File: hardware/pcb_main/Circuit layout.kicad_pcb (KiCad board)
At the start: 4 copper layers, 0 parts

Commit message: Bridges done, main layout done
layer pours done
CHanged zif connector to 8 wide to the bridge
Changed voltage levels
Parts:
- added C1: 1uF, Capacitor_SMD:C_0402_1005Metric_Pad0.74x0.62mm_HandSolder, F.Cu at (108.6, 105.3)
- added C10: 4.7nF, Capacitor_SMD:C_0402_1005Metric_Pad0.74x0.62mm_HandSolder, F.Cu at (82.2, 119.8)
- added C11: 4.7nF, Capacitor_SMD:C_0402_1005Metric_Pad0.74x0.62mm_HandSolder, F.Cu at (80.2, 119.8)
- added C12: 100nF, Capacitor_SMD:C_0402_1005Metric_Pad0.74x0.62mm_HandSolder, F.Cu at (93.0, 122.5)
- added C13: 10uF, Capacitor_SMD:C_0402_1005Metric_Pad0.74x0.62mm_HandSolder, F.Cu at (94.0, 122.5)
- added C14: 1uF, Capacitor_SMD:C_0402_1005Metric_Pad0.74x0.62mm_HandSolder, F.Cu at (95.0, 122.5)
- added C15: 100uF, Capacitor_SMD:C_0805_2012Metric_Pad1.18x1.45mm_HandSolder, F.Cu at (97.5, 122.3)
- added C16: 1uF, Capacitor_SMD:C_0402_1005Metric_Pad0.74x0.62mm_HandSolder, F.Cu at (100.0, 122.4)
- added C17: 1.5nF, Capacitor_SMD:C_0402_1005Metric_Pad0.74x0.62mm_HandSolder, F.Cu at (91.0, 107.0)
- added C18: 100nF, Capacitor_SMD:C_0402_1005Metric_Pad0.74x0.62mm_HandSolder, F.Cu at (96.5, 107.0)
- added C19: 1uF, Capacitor_SMD:C_0402_1005Metric_Pad0.74x0.62mm_HandSolder, F.Cu at (96.5, 106.0)
- added C2: 1uF, Capacitor_SMD:C_0402_1005Metric_Pad0.74x0.62mm_HandSolder, F.Cu at (105.8, 105.3)
- added C20: 100nF, Capacitor_SMD:C_0402_1005Metric_Pad0.74x0.62mm_HandSolder, F.Cu at (113.2, 110.8)
- added C21: 100pF, Capacitor_SMD:C_0402_1005Metric_Pad0.74x0.62mm_HandSolder, F.Cu at (116.2, 102.0)
- added C22: 1uF, Capacitor_SMD:C_0402_1005Metric_Pad0.74x0.62mm_HandSolder, F.Cu at (114.0, 106.3)
- added C23: 100nF, Capacitor_SMD:C_0402_1005Metric_Pad0.74x0.62mm_HandSolder, F.Cu at (123.0, 110.8)
- added C24: 0p3, Capacitor_SMD:C_0402_1005Metric, F.Cu at (119.0, 99.0)
- added C25: 0p8, Capacitor_SMD:C_0402_1005Metric, F.Cu at (119.0, 102.0)
- added C26: 12pF, Capacitor_SMD:C_0603_1608Metric_Pad1.08x0.95mm_HandSolder, F.Cu at (114.8, 100.5)
- added C27: 12pF, Capacitor_SMD:C_0603_1608Metric_Pad1.08x0.95mm_HandSolder, F.Cu at (111.2, 104.2)
- added C28: 1uF, Capacitor_SMD:C_0402_1005Metric_Pad0.74x0.62mm_HandSolder, F.Cu at (92.0, 122.5)
- added C29: 1uF, Capacitor_SMD:C_0402_1005Metric_Pad0.74x0.62mm_HandSolder, F.Cu at (91.0, 122.5)
- added C3: 4.7uF, Capacitor_SMD:C_0402_1005Metric_Pad0.74x0.62mm_HandSolder, F.Cu at (100.5, 104.3)
- added C30: 1uF, Capacitor_SMD:C_0402_1005Metric_Pad0.74x0.62mm_HandSolder, F.Cu at (90.0, 122.5)
- added C31: 1uF, Capacitor_SMD:C_0402_1005Metric_Pad0.74x0.62mm_HandSolder, F.Cu at (94.5, 106.5)
- added C32: 1uF, Capacitor_SMD:C_0402_1005Metric_Pad0.74x0.62mm_HandSolder, F.Cu at (93.0, 106.5)
- added C33: 1uF, Capacitor_SMD:C_0402_1005Metric_Pad0.74x0.62mm_HandSolder, F.Cu at (103.5, 105.8)
- added C34: 1uF, Capacitor_SMD:C_0402_1005Metric_Pad0.74x0.62mm_HandSolder, F.Cu at (101.5, 109.3)
- added C4: 1uF, Capacitor_SMD:C_0402_1005Metric_Pad0.74x0.62mm_HandSolder, F.Cu at (96.0, 104.2)
- added C5: 4.7uF, Capacitor_SMD:C_0402_1005Metric_Pad0.74x0.62mm_HandSolder, F.Cu at (100.5, 102.0)
- added C6: 1uF, Capacitor_SMD:C_0402_1005Metric_Pad0.74x0.62mm_HandSolder, F.Cu at (100.0, 100.3)
- added C7: 1uF, Capacitor_SMD:C_0402_1005Metric_Pad0.74x0.62mm_HandSolder, F.Cu at (100.0, 99.2)
- added C8: 4.7nF, Capacitor_SMD:C_0402_1005Metric_Pad0.74x0.62mm_HandSolder, F.Cu at (86.2, 119.8)
- added C9: 4.7nF, Capacitor_SMD:C_0402_1005Metric_Pad0.74x0.62mm_HandSolder, F.Cu at (83.8, 119.8)
- added FLT1: DLF162500LT-5028A1, foots:DLF162500LT-5028A1, F.Cu at (118.7, 97.5)
- added FM1: Fiducial, Fiducial:Fiducial_1mm_Mask2mm, F.Cu at (154.8, 93.8)
- added FM2: Fiducial, Fiducial:Fiducial_1mm_Mask2mm, F.Cu at (74.0, 97.5)
- added FM3: Fiducial, Fiducial:Fiducial_1mm_Mask2mm, F.Cu at (73.2, 125.5)
- added J1: 687108149022, foots:687108149022, F.Cu at (73.0, 115.3)
- added J2: PH1-06-UA, foots:PH1-06-UA, F.Cu at (107.0, 114.8)
- added J3: FTSH-105-01-L-DV-K, foots:FTSH10501LDVK, F.Cu at (130.4, 99.2)
- added J4: PH1-12-UA, foots:PH1-12-UA, F.Cu at (123.9, 107.5)
- added L1: 15nH, Inductor_SMD:L_0402_1005Metric_Pad0.77x0.64mm_HandSolder, F.Cu at (112.2, 106.8)
- added L2: 10uH, Inductor_SMD:L_1008_2520Metric_Pad1.43x2.20mm_HandSolder, F.Cu at (111.8, 108.8)
- added L3: AMCA31-2R450G-S1F-T3, foots:AMCA31-2R450G-S1F-T3, F.Cu at (119.2, 94.0)
- added L4: 2n7, Inductor_SMD:L_0402_1005Metric, F.Cu at (118.5, 100.5)
- added R1: 6.34K, Resistor_SMD:R_0402_1005Metric_Pad0.72x0.64mm_HandSolder, F.Cu at (98.6, 101.8)
- added R10: 1M, Resistor_SMD:R_0402_1005Metric_Pad0.72x0.64mm_HandSolder, F.Cu at (105.5, 107.0)
- added R11: 10K, Resistor_SMD:R_0402_1005Metric_Pad0.72x0.64mm_HandSolder, F.Cu at (107.0, 110.4)
- added R12: 10K, Resistor_SMD:R_0402_1005Metric_Pad0.72x0.64mm_HandSolder, F.Cu at (107.0, 111.4)
- added R13: 10K, Resistor_SMD:R_0402_1005Metric_Pad0.72x0.64mm_HandSolder, F.Cu at (107.0, 109.4)
- added R14: 10K, Resistor_SMD:R_0402_1005Metric_Pad0.72x0.64mm_HandSolder, F.Cu at (107.0, 112.4)
- added R15: 10K, Resistor_SMD:R_0402_1005Metric_Pad0.72x0.64mm_HandSolder, F.Cu at (109.0, 108.4)
- added R16: 10K, Resistor_SMD:R_0402_1005Metric_Pad0.72x0.64mm_HandSolder, F.Cu at (101.5, 122.5)
- added R2: 10K, Resistor_SMD:R_0402_1005Metric_Pad0.72x0.64mm_HandSolder, F.Cu at (100.0, 98.2)
- added R3: 5K, Resistor_SMD:R_0402_1005Metric_Pad0.72x0.64mm_HandSolder, F.Cu at (79.4, 113.8)
- added R4: 5K, Resistor_SMD:R_0402_1005Metric_Pad0.72x0.64mm_HandSolder, F.Cu at (79.4, 114.8)
- added R5: 5K, Resistor_SMD:R_0402_1005Metric_Pad0.72x0.64mm_HandSolder, F.Cu at (79.4, 115.8)
- added R6: 5K, Resistor_SMD:R_0402_1005Metric_Pad0.72x0.64mm_HandSolder, F.Cu at (79.4, 116.8)
- added R7: 5K, Resistor_SMD:R_0402_1005Metric_Pad0.72x0.64mm_HandSolder, F.Cu at (79.0, 119.8)
- added R8: 50K, Resistor_SMD:R_0402_1005Metric_Pad0.72x0.64mm_HandSolder, F.Cu at (85.8, 107.8)
- added R9: 1M, Resistor_SMD:R_0402_1005Metric_Pad0.72x0.64mm_HandSolder, F.Cu at (91.0, 106.0)
- added TP1: 3V, TestPoint:TestPoint_Pad_D3.0mm, B.Cu at (125.0, 119.0)
- added TP2: -2V, TestPoint:TestPoint_Pad_D3.0mm, B.Cu at (94.8, 114.3)
- added U1: 1016TR, foots:1016TR, F.Cu at (132.1, 120.1)
- added U2: TPS7A2030PDQNR, foots:TPS7A2030PDQNR, F.Cu at (107.3, 104.8)
- added U3: LM27761, foots:LM27761DSGT, F.Cu at (98.3, 103.5)
- added U4: ADS1299IPAGR, foots:ADS1299IPAGR, F.Cu at (94.2, 114.3)
- added U5: nRF52832-QFxx, foots:NRF52832-QFAA-R, F.Cu at (118.2, 107.6)
- added Y1: 32MHz, Crystal:Crystal_SMD_3225-4Pin_3.2x2.5mm_HandSoldering, F.Cu at (111.2, 100.8)
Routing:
- added copper zone on B.Cu, net +3V
- added copper zone on F.Cu, net -2V
- added copper zone on In1.Cu, net -2V
- added copper zone on In2.Cu, net GND
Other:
- board outline added: 93 x 42 mm
- rule pad_to_mask_clearance: 0 -> 0.05

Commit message: both bridge finished
main pcb layout nearly there
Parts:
- moved C30 1.60 mm to (90.0, 124.1)
- moved C10 1.28 mm to (82.0, 118.6)
- moved C11 1.28 mm to (80.0, 118.6)
- moved C8 1.28 mm to (86.0, 118.6)
- moved C9 1.28 mm to (83.5, 118.6)
- moved R7 1.28 mm to (78.8, 118.6)
- moved C29 0.83 mm to (91.0, 123.3)
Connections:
- J1 pad 1: -2V -> /EEG4R
- J1 pad 2: /EEG4R -> /EEGBIASR
- J1 pad 3: /EEG3R -> -2V
- J1 pad 4: /EEGBIASR -> /EEG3R
- J1 pad 5: /EEGREFR -> /EEG2R
- J1 pad 6: /EEG2R -> -2V
- J1 pad 7: /EEG1R -> /EEGREFR
- J1 pad 8: -2V -> /EEG1R
- U4 pad 10: unconnected-(U4-IN4P-Pad10) -> +3V
- U4 pad 12: unconnected-(U4-IN3P-Pad12) -> +3V
- U4 pad 14: unconnected-(U4-IN2P-Pad14) -> +3V
- U4 pad 16: unconnected-(U4-IN1P-Pad16) -> +3V
- U4 pad 17: unconnected-(U4-SRB1-Pad17) -> -2V
- U5 pad 10: unconnected-(U5-P0.08-Pad10) -> GND
- U5 pad 11: unconnected-(U5-NFC1/P0.09-Pad11) -> GND
- U5 pad 12: unconnected-(U5-NFC2/P0.10-Pad12) -> GND
- U5 pad 14: unconnected-(U5-P0.11-Pad14) -> GND
- U5 pad 15: unconnected-(U5-P0.12-Pad15) -> GND
- U5 pad 2: unconnected-(U5-P0.00/XL1-Pad2) -> GND
- U5 pad 3: unconnected-(U5-P0.01/XL2-Pad3) -> GND
- U5 pad 32: unconnected-(U5-DEC2-Pad32) -> GND
- U5 pad 37: unconnected-(U5-P0.25-Pad37) -> GND
- U5 pad 38: unconnected-(U5-P0.26-Pad38) -> GND
- U5 pad 39: unconnected-(U5-P0.27-Pad39) -> GND
- U5 pad 4: unconnected-(U5-P0.02/AIN0-Pad4) -> GND
- U5 pad 40: unconnected-(U5-P0.28/AIN4-Pad40) -> GND
- U5 pad 41: unconnected-(U5-P0.29/AIN5-Pad41) -> GND
- U5 pad 42: unconnected-(U5-P0.30/AIN6-Pad42) -> GND
- U5 pad 43: unconnected-(U5-P0.31/AIN7-Pad43) -> GND
- U5 pad 5: unconnected-(U5-P0.03/AIN1-Pad5) -> GND
- U5 pad 6: unconnected-(U5-P0.04/AIN2-Pad6) -> GND
- U5 pad 7: unconnected-(U5-P0.05/AIN3-Pad7) -> GND
- U5 pad 8: unconnected-(U5-P0.06-Pad8) -> GND
- U5 pad 9: unconnected-(U5-P0.07-Pad9) -> GND

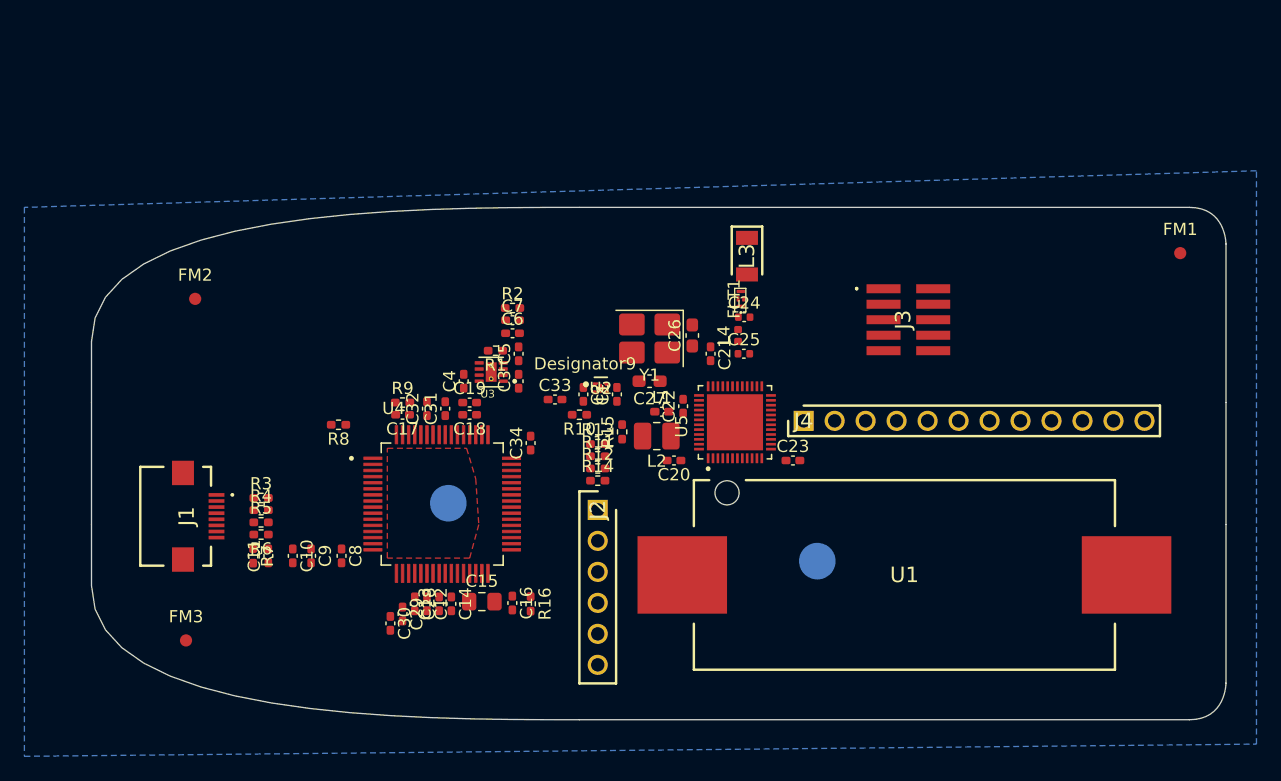
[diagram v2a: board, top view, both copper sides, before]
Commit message: layout finalised, routing started
more board fills, electrode routing done, faraday cage around electrode traces
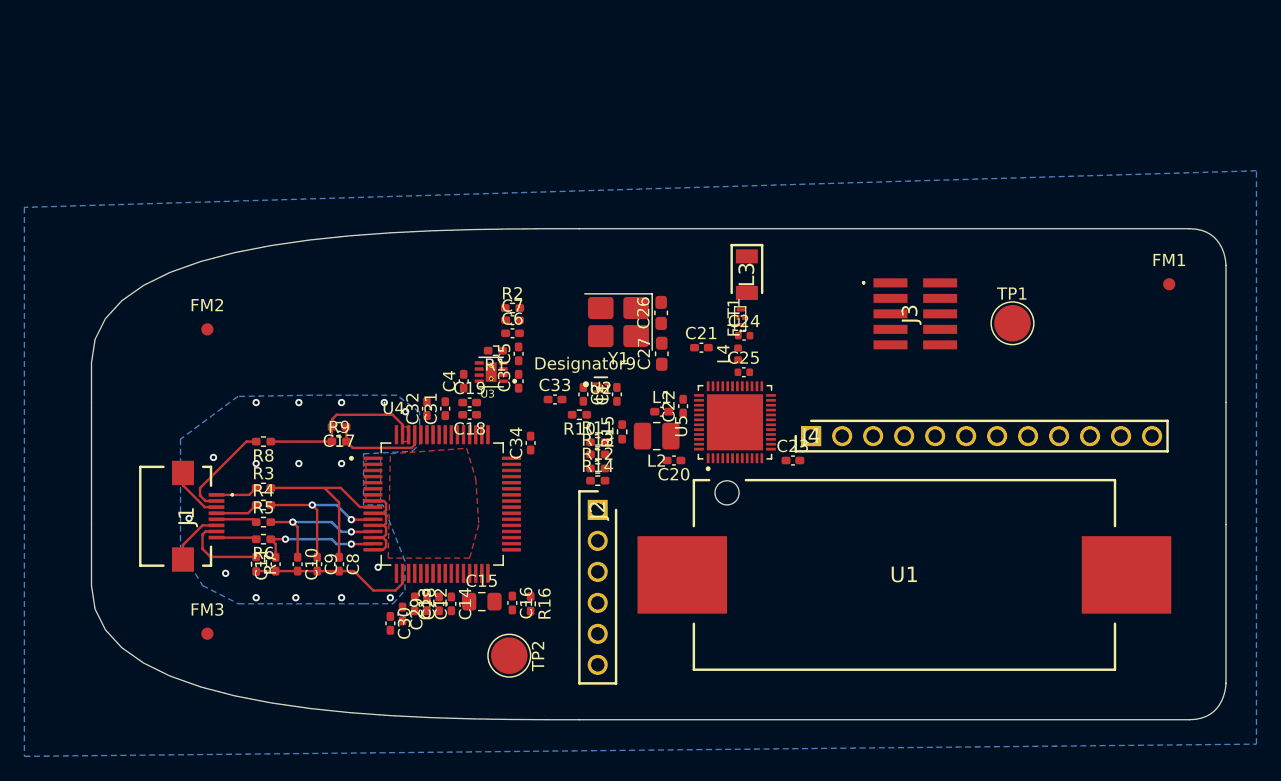
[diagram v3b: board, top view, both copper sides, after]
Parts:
- TP1, TP2: moved to F.Cu
- moved TP1 25.2 mm to (141.0, 99.5)
- moved TP2 13.5 mm to (99.8, 126.8), turned to -90 degrees
- moved R8 6.30 mm to (79.6, 109.2)
- moved R9 6.11 mm to (85.8, 109.2)
- moved C17 5.30 mm to (85.8, 108.0)
- moved C26 3.15 mm to (112.2, 98.7)
- moved Y1 2.89 mm to (108.7, 99.4)
- moved FM1 2.70 mm to (153.8, 96.3)
- moved FM2 2.69 mm to (75.0, 100.0)
- moved C27 2.46 mm to (112.2, 102.0), turned to 90 degrees
- moved FM3 1.83 mm to (75.0, 125.0)
- moved C24 1.52 mm to (119.0, 100.5)
- moved C25 1.52 mm to (119.0, 103.5)
- moved FLT1 1.52 mm to (118.7, 99.0)
- moved L3 1.52 mm to (119.2, 95.5)
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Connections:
- net /DRDY renamed /SPI_DRDY
- net /RESET renamed /SPI_RESET
- net Net-(U4-BIASINV) renamed /EEGBIASINV
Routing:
- net /EEG4: track 0.00 -> 15.2 mm
- net /EEGBIAS: track 0.00 -> 13.9 mm
- net /EEGREF: track 0.00 -> 13.7 mm
- net /EEG3: track 0.00 -> 13.3 mm, vias 0 -> 2
- net /EEG2: track 0.00 -> 11.8 mm, vias 0 -> 2
- net /EEG1: track 0.00 -> 10.2 mm, vias 0 -> 2
- net -2V: track 0.00 -> 9.12 mm, vias 0 -> 16
- net +3V: track 0.00 -> 9.07 mm
- net /EEGBIASR: track 0.00 -> 8.33 mm
- net /EEGBIASINV: track 0.00 -> 7.96 mm
- net /EEGREFR: track 0.00 -> 7.10 mm
- net /EEG3R: track 0.00 -> 3.53 mm
- net /EEG4R: track 0.00 -> 3.49 mm
- net /EEG2R: track 0.00 -> 3.35 mm
- net /EEG1R: track 0.00 -> 3.31 mm
- added copper zone on F.Cu, net +3V
- added copper zone on B.Cu, net -2V
- added copper zone on F.Cu, net /EEGBIAS
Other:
- board size 93 x 42 mm -> 93 x 40.2 mm

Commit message: Most of routing done
need to do power routing and add reverse voltage protection
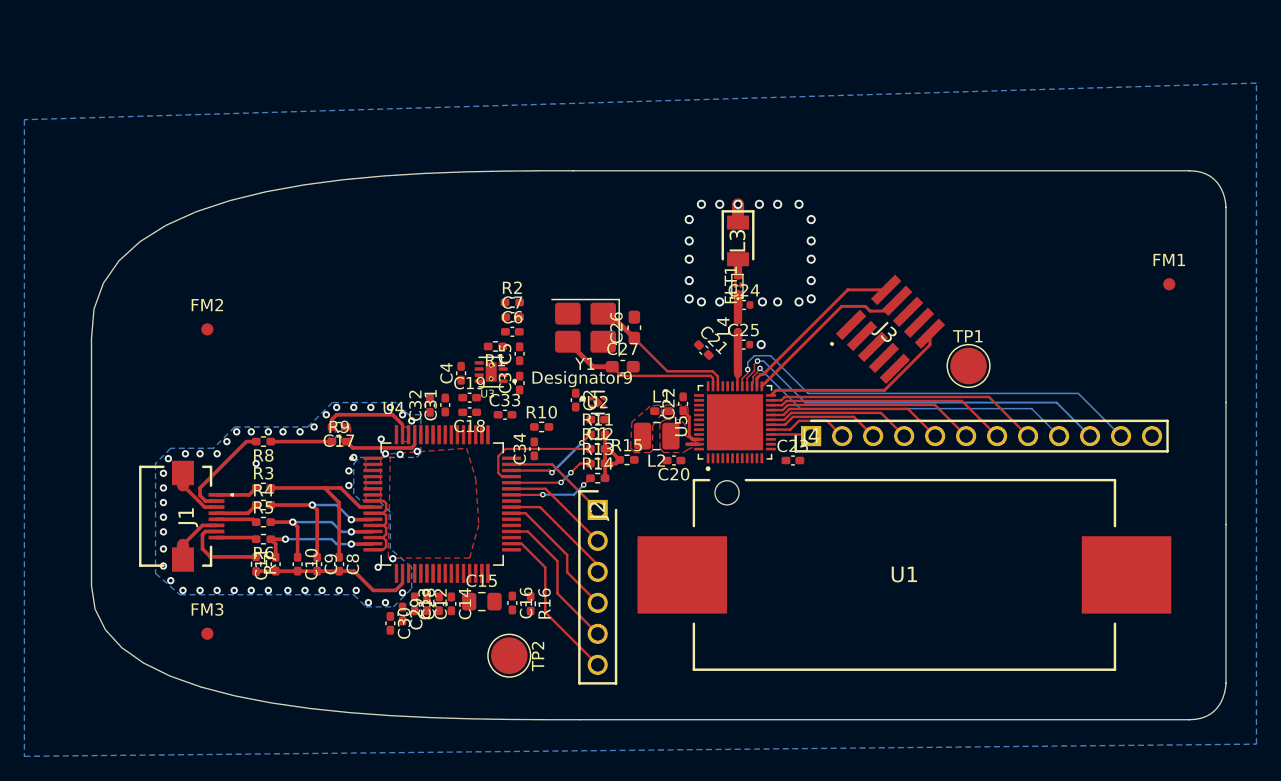
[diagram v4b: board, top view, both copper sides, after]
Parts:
- moved TP1 5.02 mm to (137.4, 103.0)
- moved C33 4.29 mm to (99.4, 107.0)
- moved C27 3.37 mm to (109.0, 103.1), turned to 0 degrees
- moved R10 3.26 mm to (102.4, 108.0), turned to 0 degrees
- moved J3 3.06 mm to (129.6, 101.4), turned to -45 degrees
- moved L3 2.86 mm to (118.5, 92.8)
- moved Y1 2.74 mm to (106.0, 99.9)
- moved FLT1 2.66 mm to (118.5, 96.4)
- moved C1 2.60 mm to (107.0, 107.4), turned to 180 degrees
- moved C24 2.52 mm to (119.0, 98.0)
- moved C26 2.51 mm to (110.0, 99.9)
- moved R15 2.33 mm to (109.4, 110.7), turned to 0 degrees
- moved C25 2.27 mm to (119.0, 101.2)
- moved L4 2.27 mm to (118.5, 99.8)
- moved R12 1.60 mm to (107.0, 109.8)
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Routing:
- net /GPIO24: track 0.00 -> 35.7 mm, vias 0 -> 1
- net /GPIO23: track 0.00 -> 32.2 mm, vias 0 -> 1
- net /GPIO22: track 0.00 -> 28.6 mm, vias 0 -> 1
- net /GPIO20: track 0.00 -> 22.5 mm
- net /GPIO19: track 0.00 -> 19.9 mm
- net /GPIO18: track 0.00 -> 17.2 mm
- net /SWRST: track 0.00 -> 15.7 mm
- net /GPIO17: track 0.00 -> 14.6 mm
- net /SWDIO: track 0.00 -> 14.5 mm
- net /SWCLK: track 0.00 -> 14.3 mm
- net /HSE_OUT: track 0.00 -> 13.8 mm
- net /SPI_MOSI: track 0.00 -> 13.3 mm
- net /HSE_IN: track 0.00 -> 12.3 mm
- net /SPI_RESET: track 0.00 -> 12.1 mm
- net /GPIO16: track 0.00 -> 11.9 mm
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- added copper zone on F.Cu, net /EEGBIASINV
- added copper zone on F.Cu, net /SMPS
- added copper zone on F.Cu, net /SMPSL
- added copper zone on F.Cu, net /SMPSLX
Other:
- board size 93 x 40.2 mm -> 93 x 45 mm
- rule pad_to_mask_clearance: 0.05 -> 0

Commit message: Most of routing done
Just GNDing left
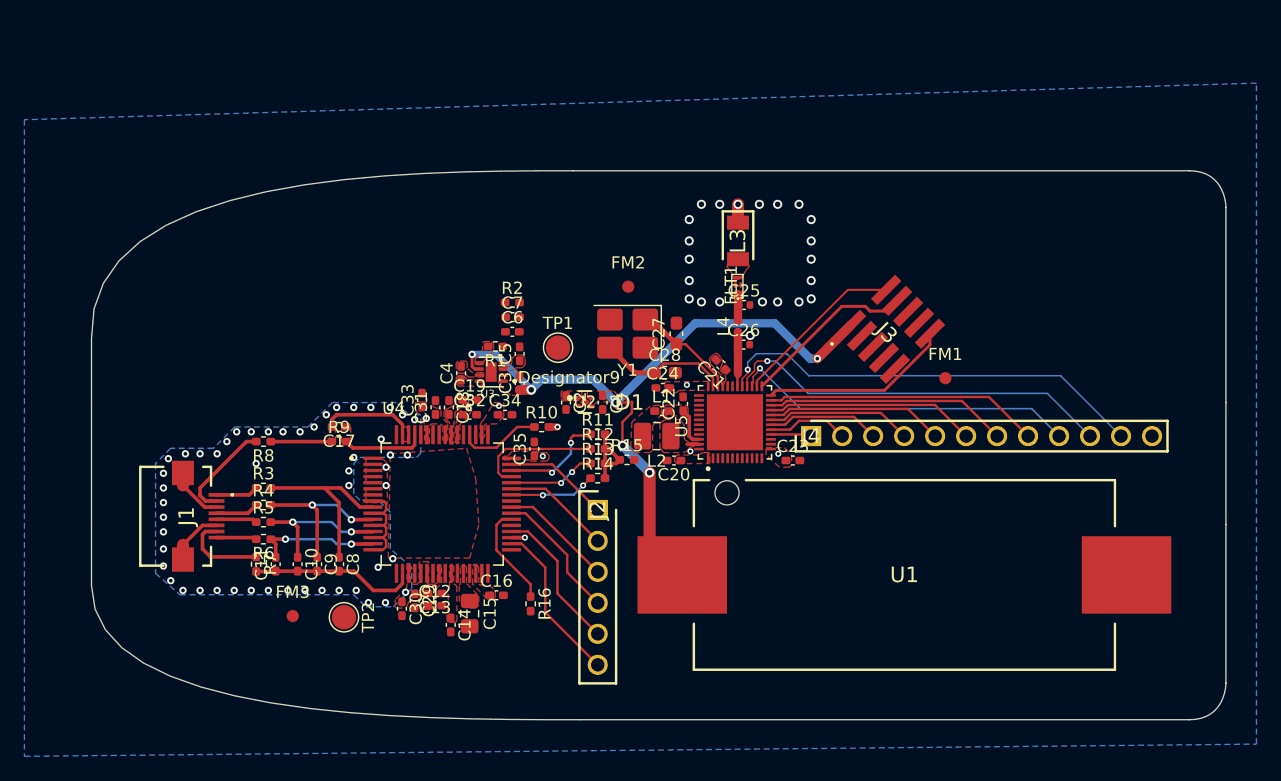
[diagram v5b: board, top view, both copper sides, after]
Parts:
- added C24: 4.7uF, Capacitor_SMD:C_0402_1005Metric_Pad0.74x0.62mm_HandSolder, F.Cu at (112.3, 104.8)
- added D1: BAT30F4, foots:BAT30F4, F.Cu at (109.6, 106.0)
- TP1, TP2: footprint TestPoint:TestPoint_Pad_D3.0mm -> TestPoint:TestPoint_Pad_D2.0mm
- U2: value TPS7A2030PDQNR -> DQN0004A-MFG
- moved FM2 34.7 mm to (109.5, 96.5)
- moved TP1 33.7 mm to (103.8, 101.5)
- moved FM1 19.9 mm to (135.5, 104.0)
- moved C31 18.1 mm to (93.7, 106.4), turned to 90 degrees
- moved TP2 13.9 mm to (86.2, 123.6)
- moved FM3 7.15 mm to (82.0, 123.5)
- moved C27 3.48 mm to (113.5, 100.3)
- moved C28 3.48 mm to (112.5, 103.5)
- moved Y1 3.48 mm to (109.5, 100.3)
- moved C32 2.15 mm to (96.5, 107.0), turned to 0 degrees
- moved C21 1.84 mm to (117.1, 102.9), turned to 135 degrees
- moved C18 1.75 mm to (94.8, 106.4), turned to -90 degrees
- moved C14 1.73 mm to (95.0, 124.2)
- moved C1 1.46 mm to (107.4, 106.0), turned to -90 degrees
- moved C16 1.45 mm to (98.7, 121.8), turned to 0 degrees
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- renumbered C24 to C25, C25 to C26, C26 to C27, C27 to C28, C28 to C29, C29 to C30, C30 to C31, C31 to C32, C32 to C33, C33 to C34, C34 to C35
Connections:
- U1 pad 1: +PWR -> /PWR_D
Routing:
- net +PWR: track 0.00 -> 41.9 mm, vias 0 -> 4
- net /PWR_D: track 0.00 -> 16.5 mm, vias 0 -> 2
- net /START: track 0.00 -> 8.46 mm
- net /CLKSEL: track 0.00 -> 6.83 mm
- net /HSE_IN: track 12.3 -> 8.68 mm
- net /HSE_OUT: track 13.8 -> 10.8 mm
- net +3V: track 9.07 -> 10.9 mm, vias 0 -> 12
- net /RF_ANT: track 1.34 -> 0.00 mm
- net /GPIO4: track 7.85 -> 8.61 mm
- net -2V: vias 50 -> 48
- added copper zone on F.Cu, net +PWR
- added copper zone on F.Cu, net /C+
- added copper zone on F.Cu, net /C-
- added copper zone on F.Cu, net /CPOUT
- added copper zone on F.Cu, net /DEC1
- added copper zone on F.Cu, net /DEC3
- added copper zone on F.Cu, net /RF_ANT
- added copper zone on F.Cu, net /VCAP1
- added copper zone on F.Cu, net /VCAP2
- added copper zone on F.Cu, net /VCAP3
- added copper zone on F.Cu, net /VCAP4
- added copper zone on F.Cu, net /VFB
- added copper zone on F.Cu, net /VREFP
